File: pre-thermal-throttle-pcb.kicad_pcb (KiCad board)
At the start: 2 copper layers, 4 parts, among them U1 CRE1S1205SC, U2 SN65HVD230, U4 ESP32-DevKitC, U5 BMI088

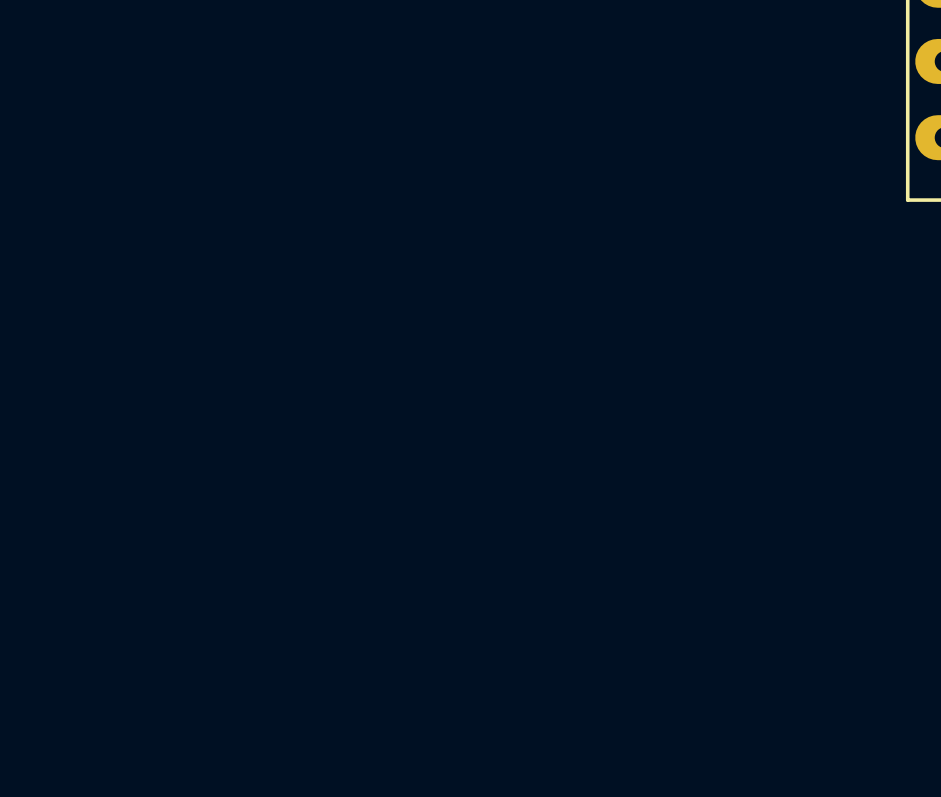
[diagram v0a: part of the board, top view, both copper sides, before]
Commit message: Add switching regulator circuit basic schematic, values need compute
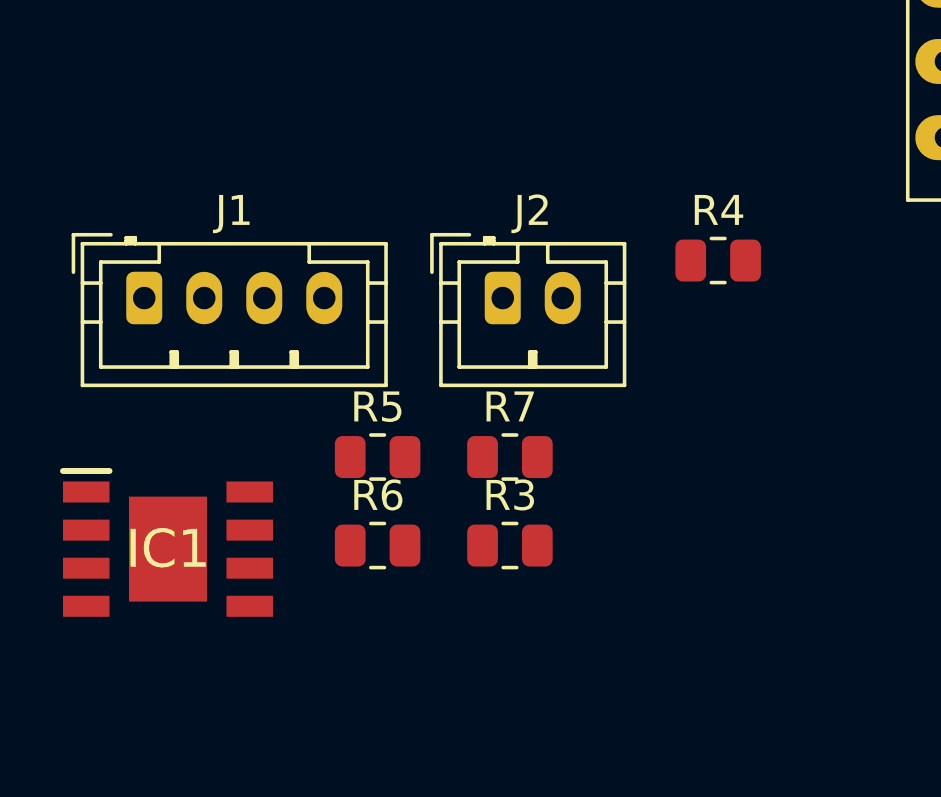
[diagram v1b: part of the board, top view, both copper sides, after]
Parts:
- added IC1: A7986ATR, A7986ATR:SOIC127P600X175-9N, F.Cu at (108.0, 112.0)
- added J1: STEERING, Connector_JST:JST_PH_B4B-PH-K_1x04_P2.00mm_Vertical, F.Cu at (107.2, 103.6)
- added J2: Motor Throttle Connector, Connector_JST:JST_PH_B2B-PH-K_1x02_P2.00mm_Vertical, F.Cu at (119.1, 103.6)
- added R3: 1.2K, Resistor_SMD:R_0805_2012Metric, F.Cu at (119.3, 111.9)
- added R4: 1.2K, Resistor_SMD:R_0805_2012Metric, F.Cu at (126.3, 102.4)
- added R5: 1.2K, Resistor_SMD:R_0805_2012Metric, F.Cu at (114.9, 108.9)
- added R6: 1.2K, Resistor_SMD:R_0805_2012Metric, F.Cu at (114.9, 111.9)
- added R7: 1M, Resistor_SMD:R_0805_2012Metric, F.Cu at (119.3, 108.9)
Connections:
- U2 pad 1: Net-(P1-Pad1) -> CAN_TXD
- U2 pad 2: Net-(P1-Pad3) -> GND
- U2 pad 3: Net-(P1-Pad4) -> +3.3V
- U2 pad 4: Net-(P1-Pad2) -> CAN_RXD
- U2 pad 8: Net-(P1-Pad3) -> Net-(R1-Pad1)
- U4 pad 1: unconnected-(U4-Pad1) -> +3.3V
- U4 pad 10: unconnected-(U4-Pad10) -> CAN_RXD
- U4 pad 14: unconnected-(U4-Pad14) -> GND
- U4 pad 19: unconnected-(U4-Pad19) -> +5V
- U4 pad 27: unconnected-(U4-Pad27) -> RXD2
- U4 pad 28: unconnected-(U4-Pad28) -> TXD2
- U4 pad 30: unconnected-(U4-Pad30) -> ESP SPI CLK
- U4 pad 31: unconnected-(U4-Pad31) -> ESP CIPO
- U4 pad 32: unconnected-(U4-Pad32) -> GND
- U4 pad 33: unconnected-(U4-Pad33) -> ESP Accel 
- U4 pad 36: unconnected-(U4-Pad36) -> ESP Gyro CS
- U4 pad 37: unconnected-(U4-Pad37) -> ESP COPI
- U4 pad 38: unconnected-(U4-Pad38) -> GND
- U4 pad 4: unconnected-(U4-Pad4) -> ESP ADC CS
- U4 pad 9: unconnected-(U4-Pad9) -> CAN_TXD
- U5 pad 10: ESP MISO -> ESP CIPO
- U5 pad 15: ESP MISO -> ESP CIPO
- U5 pad 9: ESP MOSI -> ESP COPI

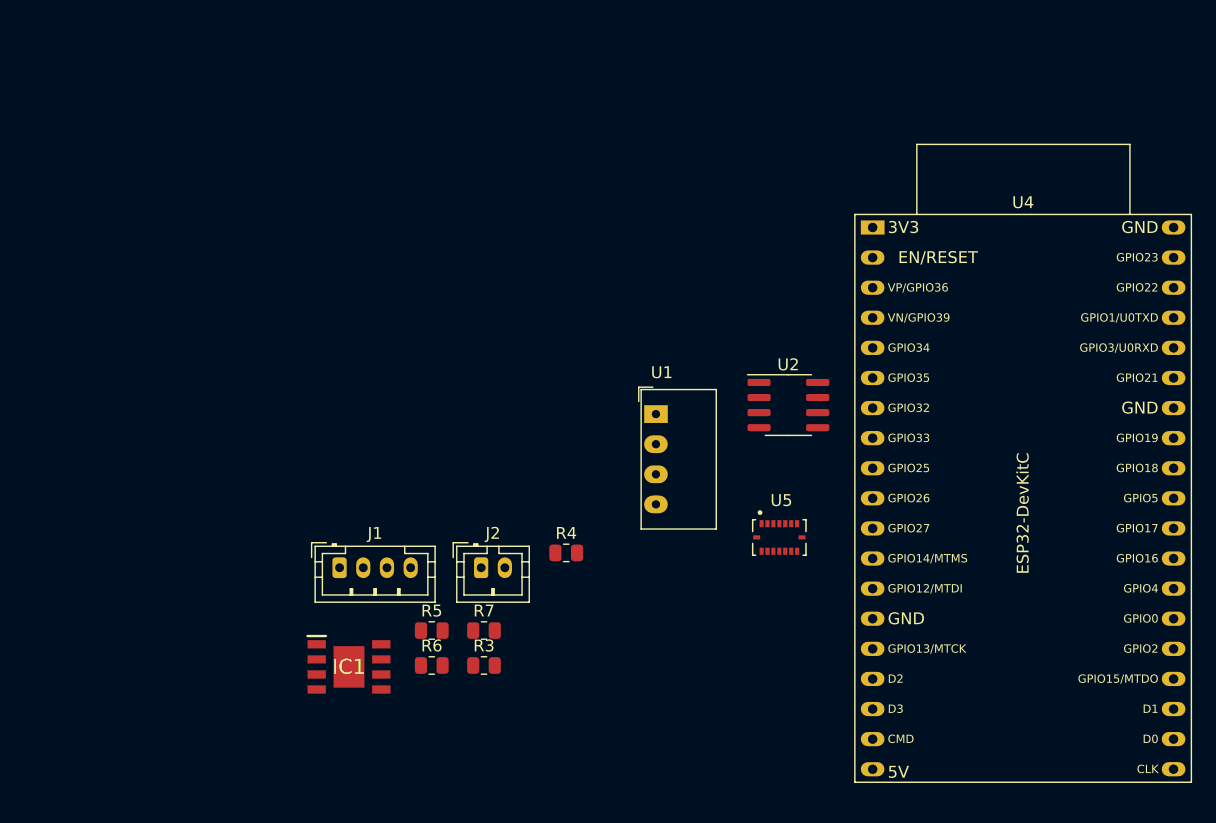
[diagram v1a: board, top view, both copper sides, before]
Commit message: Setup footprints and add bypass caps
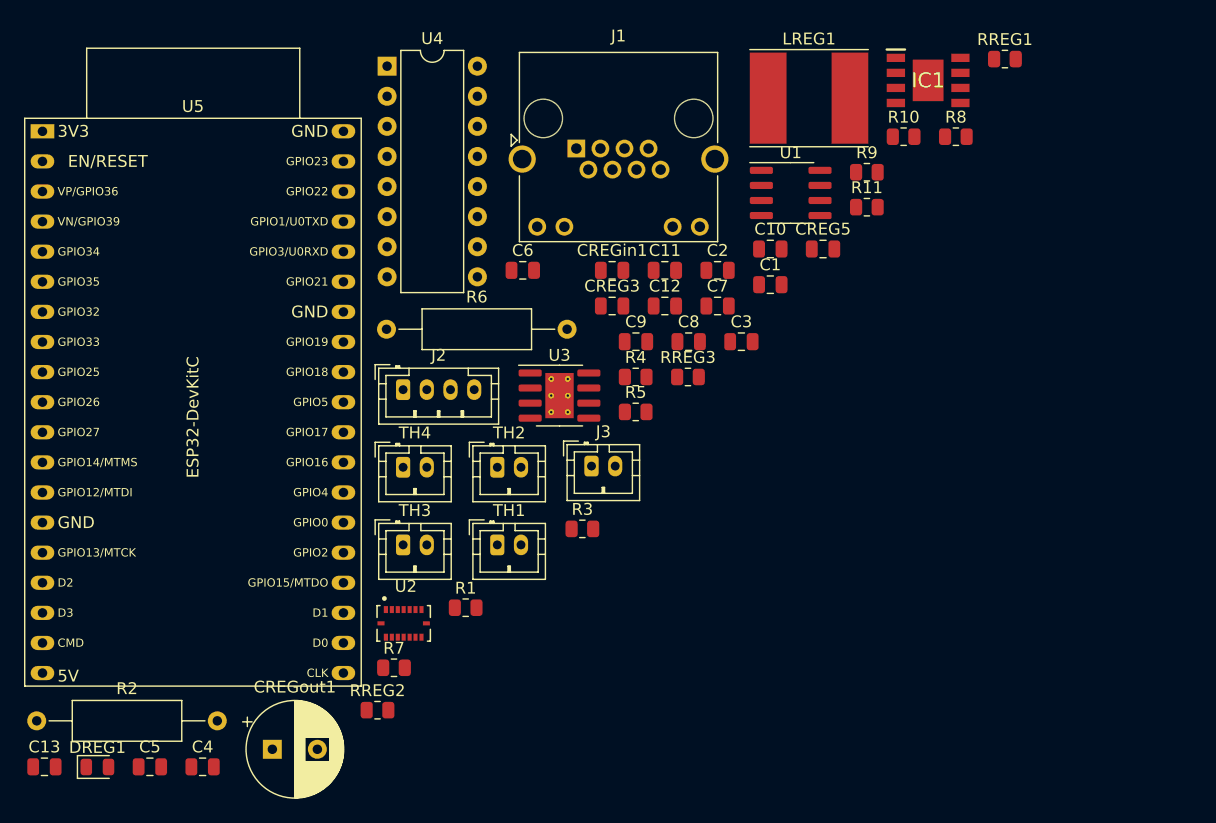
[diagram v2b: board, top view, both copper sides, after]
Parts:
- added C1: 100 nF, Capacitor_SMD:C_0805_2012Metric, F.Cu at (143.5, 79.8)
- added C10: 100 nF, Capacitor_SMD:C_0805_2012Metric, F.Cu at (143.5, 76.7)
- added C11: 100 nF, Capacitor_SMD:C_0805_2012Metric, F.Cu at (134.6, 78.5)
- added C12: 100 nF, Capacitor_SMD:C_0805_2012Metric, F.Cu at (134.6, 81.6)
- added C13: 100 nF, Capacitor_SMD:C_0805_2012Metric, F.Cu at (82.2, 120.4)
- added C2: 100 nF, Capacitor_SMD:C_0805_2012Metric, F.Cu at (139.1, 78.5)
- added C3: 100 nF, Capacitor_SMD:C_0805_2012Metric, F.Cu at (141.1, 84.6)
- added C4: 100 nF, Capacitor_SMD:C_0805_2012Metric, F.Cu at (95.6, 120.4)
- added C5: 100 nF, Capacitor_SMD:C_0805_2012Metric, F.Cu at (91.2, 120.4)
- added C6: 100 nF, Capacitor_SMD:C_0805_2012Metric, F.Cu at (122.6, 78.5)
- added C7: 100 nF, Capacitor_SMD:C_0805_2012Metric, F.Cu at (139.1, 81.6)
- added C8: 100 nF, Capacitor_SMD:C_0805_2012Metric, F.Cu at (136.6, 84.6)
- added C9: 100 nF, Capacitor_SMD:C_0805_2012Metric, F.Cu at (132.2, 84.6)
- added CREG3: C, Capacitor_SMD:C_0805_2012Metric, F.Cu at (130.2, 81.6)
- added CREG5: C, Capacitor_SMD:C_0805_2012Metric, F.Cu at (148.0, 76.7)
- added CREGin1: C, Capacitor_SMD:C_0805_2012Metric, F.Cu at (130.2, 78.5)
- added CREGout1: C_Polarized, Capacitor_THT:CP_Radial_D8.0mm_P3.80mm, F.Cu at (101.5, 119.0)
- added DREG1: D, Diode_SMD:D_0805_2012Metric, F.Cu at (86.7, 120.5)
- added J3: Motor Throttle Connector, Connector_JST:JST_PH_B2B-PH-K_1x02_P2.00mm_Vertical, F.Cu at (128.4, 95.1)
- added LREG1: L, Inductor_SMD:L_Taiyo-Yuden_NR-80xx_HandSoldering, F.Cu at (146.8, 64.0)
- added R1: 10K, Resistor_SMD:R_0805_2012Metric, F.Cu at (117.8, 107.0)
- added R10: 1.2K, Resistor_SMD:R_0805_2012Metric, F.Cu at (154.8, 67.3)
- added R11: 1M, Resistor_SMD:R_0805_2012Metric, F.Cu at (151.7, 73.2)
- added R2: 120R, Resistor_THT:R_Axial_DIN0309_L9.0mm_D3.2mm_P15.24mm_Horizontal, F.Cu at (81.6, 116.6)
- added R8: 1.2K, Resistor_SMD:R_0805_2012Metric, F.Cu at (159.2, 67.3)
- added R9: 1.2K, Resistor_SMD:R_0805_2012Metric, F.Cu at (151.7, 70.3)
- added RREG1: R, Resistor_SMD:R_0805_2012Metric, F.Cu at (163.3, 60.7)
- added RREG2: R, Resistor_SMD:R_0805_2012Metric, F.Cu at (110.4, 115.7)
- added RREG3: R, Resistor_SMD:R_0805_2012Metric, F.Cu at (136.6, 87.5)
- added TH1: PTFM102 Thermistor, Connector_JST:JST_PH_B2B-PH-K_1x02_P2.00mm_Vertical, F.Cu at (120.5, 101.7)
- added TH2: PTFM102 Thermistor, Connector_JST:JST_PH_B2B-PH-K_1x02_P2.00mm_Vertical, F.Cu at (120.5, 95.2)
- added TH3: PTFM102 Thermistor, Connector_JST:JST_PH_B2B-PH-K_1x02_P2.00mm_Vertical, F.Cu at (112.5, 101.7)
- added TH4: PTFM102 Thermistor, Connector_JST:JST_PH_B2B-PH-K_1x02_P2.00mm_Vertical, F.Cu at (112.5, 95.2)
- added U3: MAX3485CSA, Package_SO:SOIC-8-1EP_3.9x4.9mm_P1.27mm_EP2.41x3.81mm_ThermalVias, F.Cu at (125.7, 89.1)
- J1: value STEERING -> RJHSE-5381-ND; footprint Connector_JST:JST_PH_B4B-PH-K_1x04_P2.00mm_Vertical -> Connector_RJ:RJ45_Amphenol_RJHSE538X
- J2: value Motor Throttle Connector -> STEERING; footprint Connector_JST:JST_PH_B2B-PH-K_1x02_P2.00mm_Vertical -> Connector_JST:JST_PH_B4B-PH-K_1x04_P2.00mm_Vertical
- R3, R5: value 1.2K -> 130R
- R4: value 1.2K -> 10K
- R6: value 1.2K -> 120R; footprint Resistor_SMD:R_0805_2012Metric -> Resistor_THT:R_Axial_DIN0309_L9.0mm_D3.2mm_P15.24mm_Horizontal
- R7: value 1M -> 1.2K
- U1: value CRE1S1205SC -> SN65HVD230; footprint Converter_DCDC:Converter_DCDC_Murata_CRE1xxxxxxSC_THT -> Package_SO:SOIC-8_3.9x4.9mm_P1.27mm
- U2: value SN65HVD230 -> BMI088; footprint Package_SO:SOIC-8_3.9x4.9mm_P1.27mm -> bmi088:PQFN50P450X300X100-16N
- U4: value ESP32-DevKitC -> MCP3008; footprint Espressif:ESP32-DevKitC -> Package_DIP:DIP-16_W7.62mm
- U5: value BMI088 -> ESP32-DevKitC; footprint bmi088:PQFN50P450X300X100-16N -> Espressif:ESP32-DevKitC
- moved U5 71.0 mm to (82.1, 66.8)
- moved IC1 69.6 mm to (156.8, 62.5)
- moved U4 43.2 mm to (111.2, 61.3)
- moved J1 40.6 mm to (127.1, 68.3)
- moved U2 37.3 mm to (112.6, 108.3)
- moved R6 28.6 mm to (111.1, 83.5)
- moved R5 25.2 mm to (132.2, 90.5)
- moved U1 21.9 mm to (145.2, 72.0)
- moved J2 16.4 mm to (112.5, 88.6)
- moved R4 16.0 mm to (132.2, 87.5)
- moved R3 14.2 mm to (127.7, 100.4)
- moved R7 8.22 mm to (111.8, 112.1)
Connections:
- IC1 pad 1: unconnected-(IC1-Pad1) -> Net-(DREG1-Pad1)
- IC1 pad 3: unconnected-(IC1-Pad3) -> +12V
- IC1 pad 4: unconnected-(IC1-Pad4) -> Net-(CREG5-Pad2)
- IC1 pad 5: unconnected-(IC1-Pad5) -> Net-(CREG3-Pad2)
- IC1 pad 7: unconnected-(IC1-Pad7) -> GND
- IC1 pad 8: unconnected-(IC1-Pad8) -> +12V
- J1 pad 1: +5V -> CAR_CANH
- J1 pad 2: STEERING_A -> CAR_CANL
- J1 pad 3: STEERING_B -> unconnected-(J1-Pad3)
- J1 pad 4: GND -> +12V
- J2 pad 1: THROTTLE_SIG -> +5V
- J2 pad 2: GND -> STEERING_A
- R3 pad 1: Net-(U3-Pad1) -> GND
- R3 pad 2: GND -> Net-(J1-Pad11)
- R4 pad 1: Net-(U3-Pad3) -> ESP_OK_LED
- R5 pad 1: Net-(U3-Pad2) -> GND
- R5 pad 2: GND -> Net-(J1-Pad9)
- R6 pad 1: Net-(U3-Pad4) -> STEERING_B
- R6 pad 2: GND -> STEERING_A
- R7 pad 1: THROTTLE_SIG -> Net-(R7-Pad1)
- U1 pad 1: GND -> CAN_TXD
- U1 pad 2: +12V -> GND
- U1 pad 3: GND1 -> +3.3V
- U1 pad 4: +5V -> CAN_RXD
- U2 pad 1: CAN_TXD -> unconnected-(U2-Pad1)
- U2 pad 4: CAN_RXD -> GND
- U2 pad 5: unconnected-(U2-Pad5) -> ESP Gyro CS
- U2 pad 6: Net-(R2-Pad2) -> GND
- U2 pad 7: Net-(R2-Pad1) -> GND
- U2 pad 8: Net-(R1-Pad1) -> ESP SPI CLK
- U4 pad 1: +3.3V -> Net-(R7-Pad1)
- U4 pad 10: CAN_RXD -> ESP ADC CS
- U4 pad 11: unconnected-(U4-Pad11) -> ESP COPI
- U4 pad 12: unconnected-(U4-Pad12) -> ESP CIPO
- U4 pad 13: unconnected-(U4-Pad13) -> ESP SPI CLK
- U4 pad 15: unconnected-(U4-Pad15) -> +5V
- U4 pad 16: unconnected-(U4-Pad16) -> +3.3V
- U4 pad 2: unconnected-(U4-Pad2) -> Net-(R9-Pad1)
- U4 pad 3: unconnected-(U4-Pad3) -> Net-(R8-Pad1)
- U4 pad 4: ESP ADC CS -> Net-(R10-Pad1)
- U4 pad 5: unconnected-(U4-Pad5) -> THROTTLE_SIG
- U4 pad 9: CAN_TXD -> GND
- U5 pad 1: unconnected-(U5-Pad1) -> +3.3V
- U5 pad 10: ESP CIPO -> CAN_RXD
- U5 pad 11: +3.3V -> unconnected-(U5-Pad11)
- U5 pad 14: ESP Accel  -> GND
- U5 pad 15: ESP CIPO -> unconnected-(U5-Pad15)
- U5 pad 2: GND -> unconnected-(U5-Pad2)
- U5 pad 3: +3.3V -> ESP_OK_LED
- U5 pad 4: GND -> ESP ADC CS
- U5 pad 5: ESP Gyro CS -> RS485 RTS
- U5 pad 6: GND -> unconnected-(U5-Pad6)
- U5 pad 7: GND -> unconnected-(U5-Pad7)
- U5 pad 8: ESP SPI CLK -> unconnected-(U5-Pad8)
- U5 pad 9: ESP COPI -> CAN_TXD

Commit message: Finish part selection
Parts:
- removed CREG3, CREG5: C, Capacitor_SMD:C_0805_2012Metric
- removed DREG1: D, Diode_SMD:D_0805_2012Metric
- removed RREG1, RREG2, RREG3: R, Resistor_SMD:R_0805_2012Metric
- added C14: 100 nF, Capacitor_SMD:C_0805_2012Metric, F.Cu at (147.4, 112.7)
- added C15: 100 nF, Capacitor_SMD:C_0805_2012Metric, F.Cu at (171.6, 112.7)
- added C16: 100 nF, Capacitor_SMD:C_0805_2012Metric, F.Cu at (159.5, 112.7)
- added C17: 100 nF, Capacitor_SMD:C_0805_2012Metric, F.Cu at (183.7, 112.7)
- added C18: 100 nF, Capacitor_SMD:C_0805_2012Metric, F.Cu at (146.5, 117.5)
- added C19: 100 nF, Capacitor_SMD:C_0805_2012Metric, F.Cu at (166.2, 117.5)
- added C20: 100 nF, Capacitor_SMD:C_0805_2012Metric, F.Cu at (154.1, 117.5)
- added C21: 100 nF, Capacitor_SMD:C_0805_2012Metric, F.Cu at (178.3, 117.5)
- added CREGboot1: 100nF, Capacitor_SMD:C_0805_2012Metric, F.Cu at (170.8, 81.9)
- added CREGin2: 1uF, Capacitor_SMD:C_0805_2012Metric, F.Cu at (168.0, 76.8)
- added CREGin3: 1uF, Capacitor_SMD:C_0805_2012Metric, F.Cu at (168.0, 78.7)
- added CREGinx1: 100nF, Capacitor_SMD:C_0805_2012Metric, F.Cu at (168.0, 73.0)
- added H1: MountingHole_Pad, MountingHole:MountingHole_3mm_Pad_Via, F.Cu at (141.0, 57.1)
- added H2: MountingHole_Pad, MountingHole:MountingHole_3mm_Pad_Via, F.Cu at (226.7, 56.5)
- added H3: MountingHole_Pad, MountingHole:MountingHole_3mm_Pad_Via, F.Cu at (228.0, 130.2)
- added H4: MountingHole_Pad, MountingHole:MountingHole_3mm_Pad_Via, F.Cu at (142.2, 130.2)
- added IC2: ADR02BRZ-REEL7, ADR02BRZ:SOIC127P600X175-8N, F.Cu at (142.2, 113.0)
- added IC3: ADR02BRZ-REEL7, ADR02BRZ:SOIC127P600X175-8N, F.Cu at (166.4, 113.0)
- added IC4: ADR02BRZ-REEL7, ADR02BRZ:SOIC127P600X175-8N, F.Cu at (154.3, 113.0)
- added IC5: ADR02BRZ-REEL7, ADR02BRZ:SOIC127P600X175-8N, F.Cu at (178.4, 113.0)
- added RREGfbb1: 22.1k, Resistor_SMD:R_0805_2012Metric, F.Cu at (172.1, 70.1)
- added RREGfbt1: 100k, Resistor_SMD:R_0805_2012Metric, F.Cu at (175.0, 69.2)
- CREGin1: value C -> 1uF
- CREGout1: value C_Polarized -> 47uF; footprint Capacitor_THT:CP_Radial_D8.0mm_P3.80mm -> Capacitor_SMD:C_0805_2012Metric
- IC1: value A7986ATR -> LMR51420XFDDCR; footprint A7986ATR:SOIC127P600X175-9N -> LMR51420XFDDCR:SOT95P280X110-6N
- J2: footprint Connector_JST:JST_PH_B4B-PH-K_1x04_P2.00mm_Vertical -> Connector_JST:JST_XH_B4B-XH-A_1x04_P2.50mm_Vertical
- J3, TH1, TH2, TH3, TH4: footprint Connector_JST:JST_PH_B2B-PH-K_1x02_P2.00mm_Vertical -> Connector_JST:JST_XH_B2B-XH-A_1x02_P2.50mm_Vertical
- LREG1: value L -> 6uH SRP1265A-6R0M; footprint Inductor_SMD:L_Taiyo-Yuden_NR-80xx_HandSoldering -> libraries:L_Bourns_SRP1260A
- U3: footprint Package_SO:SOIC-8-1EP_3.9x4.9mm_P1.27mm_EP2.41x3.81mm_ThermalVias -> libraries:SOIC-8-1EP_3.9x4.9mm_P1.27mm_EP2.41x3.81mm_ThermalVias
- moved C13 131.1 mm to (202.9, 69.2)
- moved U5 119.6 mm to (201.6, 72.2)
- moved R6 90.5 mm to (198.1, 58.4), turned to 180 degrees
- moved CREGout1 90.1 mm to (174.0, 65.4)
- moved J2 84.7 mm to (189.3, 52.7)
- moved C12 78.2 mm to (201.9, 121.3)
- moved C5 77.7 mm to (159.3, 83.2), turned to 90 degrees
- moved U4 74.9 mm to (170.8, 106.7), turned to 90 degrees
- moved U2 74.9 mm to (185.4, 90.8), turned to -90 degrees
- moved TH4 73.9 mm to (181.1, 122.6), turned to 180 degrees
- moved U3 71.8 mm to (193.1, 64.1), turned to 90 degrees
- moved C4 71.6 mm to (156.7, 83.2), turned to 90 degrees
- moved J3 69.6 mm to (192.4, 122.5), turned to 180 degrees
- moved C6 67.7 mm to (189.2, 90.8), turned to -90 degrees
- moved R2 61.9 mm to (139.7, 95.2)
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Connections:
- IC1 pad 1: Net-(DREG1-Pad1) -> GND
- IC1 pad 2: unconnected-(IC1-Pad2) -> Net-(CREGboot1-Pad2)
- IC1 pad 5: Net-(CREG3-Pad2) -> +12V
- IC1 pad 6: unconnected-(IC1-Pad6) -> Net-(CREGboot1-Pad1)
- LREG1 pad 1: Net-(DREG1-Pad1) -> Net-(CREGboot1-Pad2)
- R10 pad 1: Net-(R10-Pad1) -> ADC_CH4
- R7 pad 1: Net-(R7-Pad1) -> ADC_CH0
- R8 pad 1: Net-(R8-Pad1) -> ADC_CH2
- R9 pad 1: Net-(R9-Pad1) -> ADC_CH1
- TH1 pad 1: +5V -> ADC_CH0
- TH1 pad 2: Net-(R7-Pad1) -> Net-(C18-Pad2)
- TH2 pad 1: +5V -> ADC_CH2
- TH2 pad 2: Net-(R8-Pad1) -> Net-(C19-Pad2)
- TH3 pad 1: +5V -> ADC_CH1
- TH3 pad 2: Net-(R9-Pad1) -> Net-(C20-Pad2)
- TH4 pad 1: +5V -> ADC_CH4
- TH4 pad 2: Net-(R10-Pad1) -> Net-(C21-Pad2)
- U4 pad 1: Net-(R7-Pad1) -> ADC_CH0
- U4 pad 2: Net-(R9-Pad1) -> ADC_CH1
- U4 pad 3: Net-(R8-Pad1) -> ADC_CH2
- U4 pad 4: Net-(R10-Pad1) -> ADC_CH3
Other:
- board outline added: 101.6 x 89.5 mm
